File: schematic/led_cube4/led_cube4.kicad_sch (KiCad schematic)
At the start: 47 parts, among them J2 Conn_01x08_Pin, J3 Conn_02x08_Counter_Clockwise, J4 Conn_02x08_Counter_Clockwise, Q1 BC338, Q2 BC338, Q3 BC338, Q4 BC338, SW1 SW_Push, SW2 SW_Push, SW3 SW_Push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

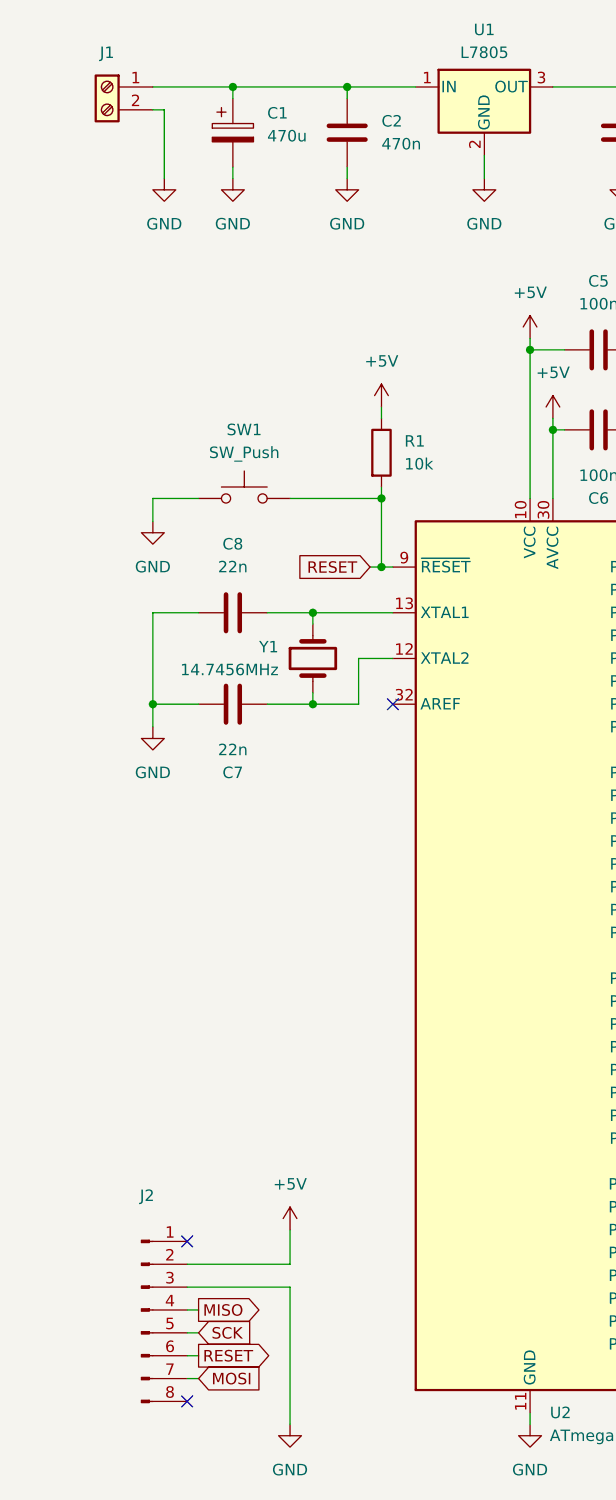
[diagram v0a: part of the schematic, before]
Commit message: fix(schematic): add 100nF capacitor to AREF pin
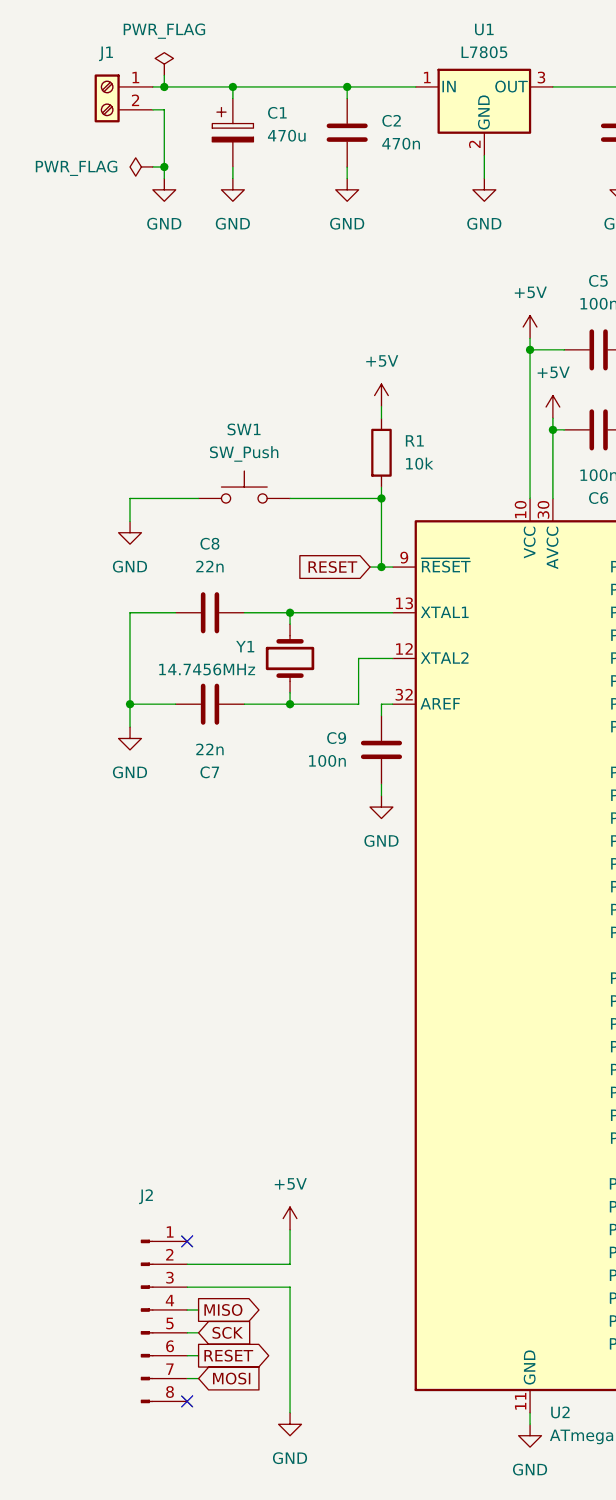
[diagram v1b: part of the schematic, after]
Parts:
- added C9: 100n, symbol Device:C
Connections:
- net GND: now also C9.2
- net at U2.32 (AREF): now also C9.1
- no-connect marks 20 -> 19
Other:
- moved on the sheet: C7, C8, Y1

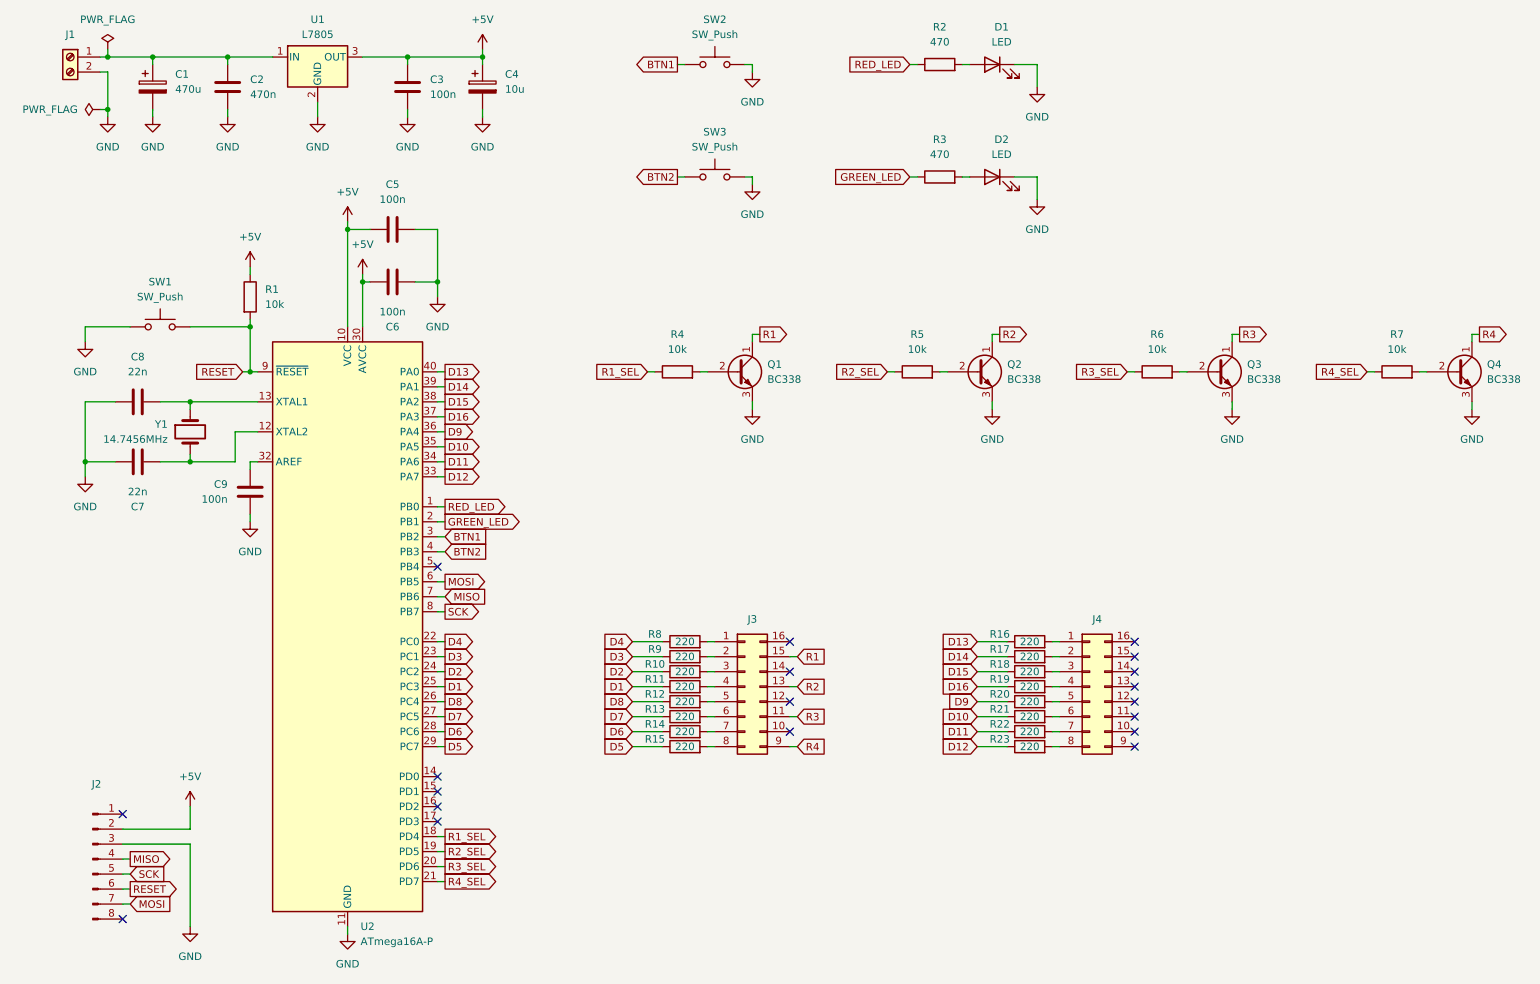
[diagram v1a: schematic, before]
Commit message: feat(schematic): add LED cube circuit
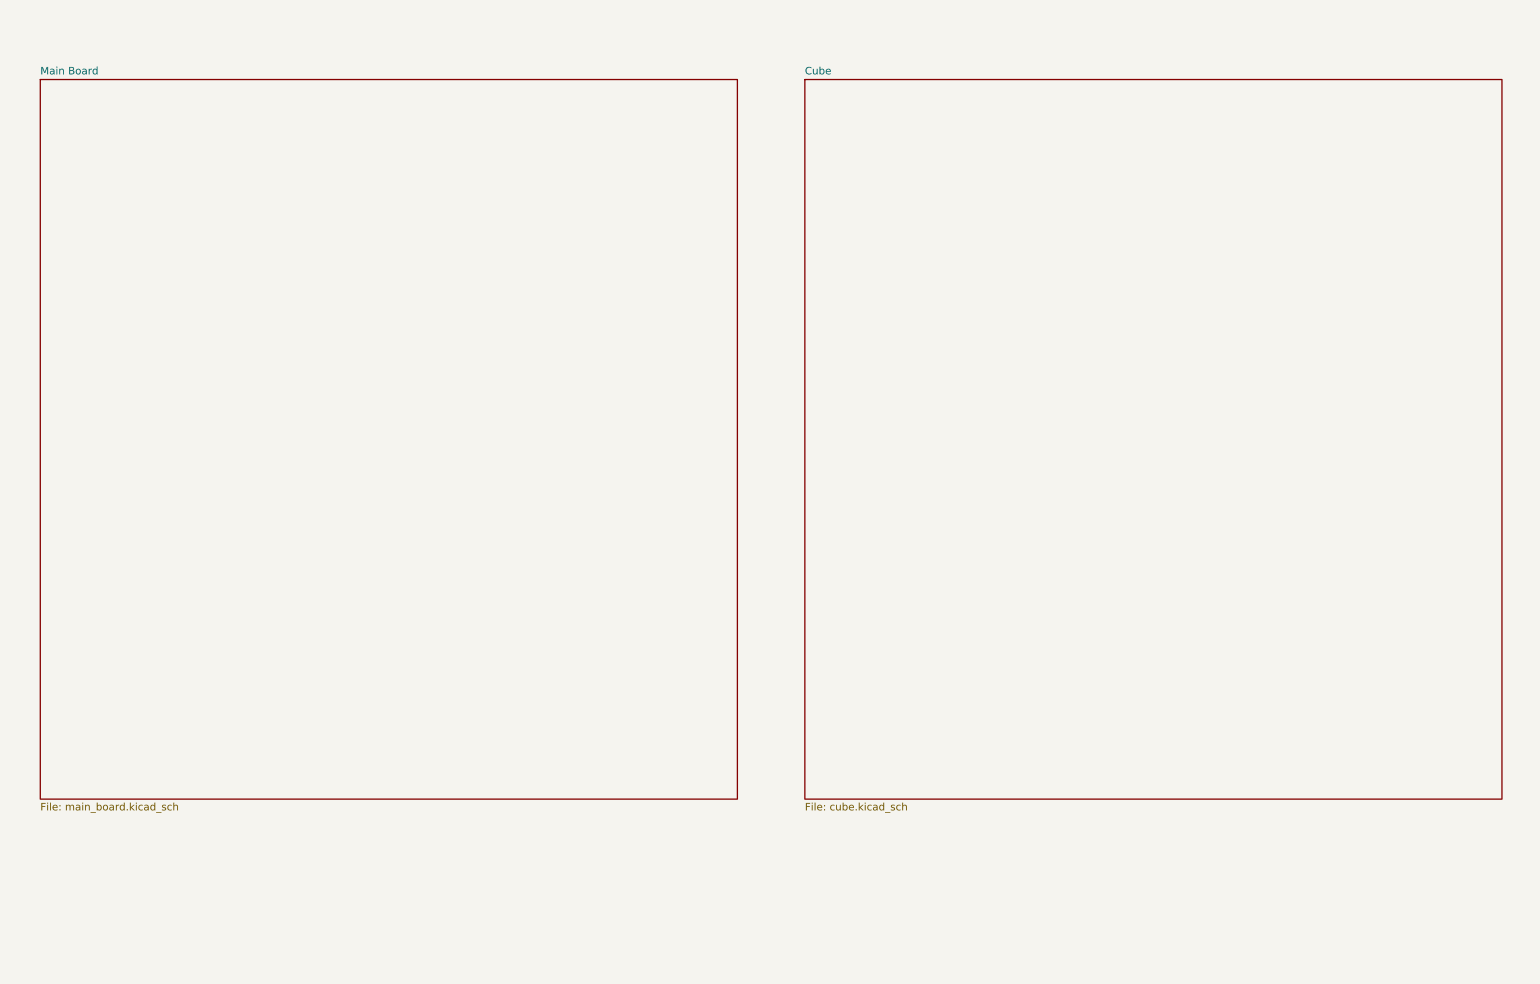
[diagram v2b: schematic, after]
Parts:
- removed C1: 470u, symbol Device:C_Polarized
- removed C2: 470n, symbol Device:C
- removed C3, C5, C6, C9: 100n, symbol Device:C
- removed C4: 10u, symbol Device:C_Polarized
- removed C7, C8: 22n, symbol Device:C
- removed D1, D2: LED, symbol Device:LED
- removed J1: ~, symbol Connector:Screw_Terminal_01x02
- removed J2: Conn_01x08_Pin, symbol Connector:Conn_01x08_Pin
- removed J3, J4: Conn_02x08_Counter_Clockwise, symbol Connector_Generic:Conn_02x08_Counter_Clockwise
- removed Q1, Q2, Q3, Q4: BC338, Package_TO_SOT_THT:TO-92_Inline, symbol Transistor_BJT:BC338
- removed R1, R4, R5, R6, R7: 10k, symbol Device:R
- removed R10, R11, R12, R13, R14, R15, R16, R17, R18, R19, R20, R21, R22, R23, R8, R9: 220, symbol Device:R
- removed R2, R3: 470, symbol Device:R
- removed SW1, SW2, SW3: SW_Push, symbol Switch:SW_Push
- removed U1: L7805, symbol Regulator_Linear:L7805
- removed U2: ATmega16A-P, Package_DIP:DIP-40_W15.24mm, symbol MCU_Microchip_ATmega:ATmega16A-P
- removed Y1: 14.7456MHz, Crystal:Crystal_AT310_D3.0mm_L10.0mm_Horizontal, symbol Device:Crystal
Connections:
- no-connect marks 19 -> 0
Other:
- added sheet Cube (cube.kicad_sch)
- added sheet Main Board (main_board.kicad_sch)
